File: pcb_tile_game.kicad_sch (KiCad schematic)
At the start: 40 parts, among them J1 Conn_01x05_Pin, J2 Conn_01x05_Socket, J3 Conn_01x05_Pin, J4 Conn_01x05_Socket, J5 Conn_01x05_Pin, J6 Conn_01x05_Socket, U2 ATtiny3217-M

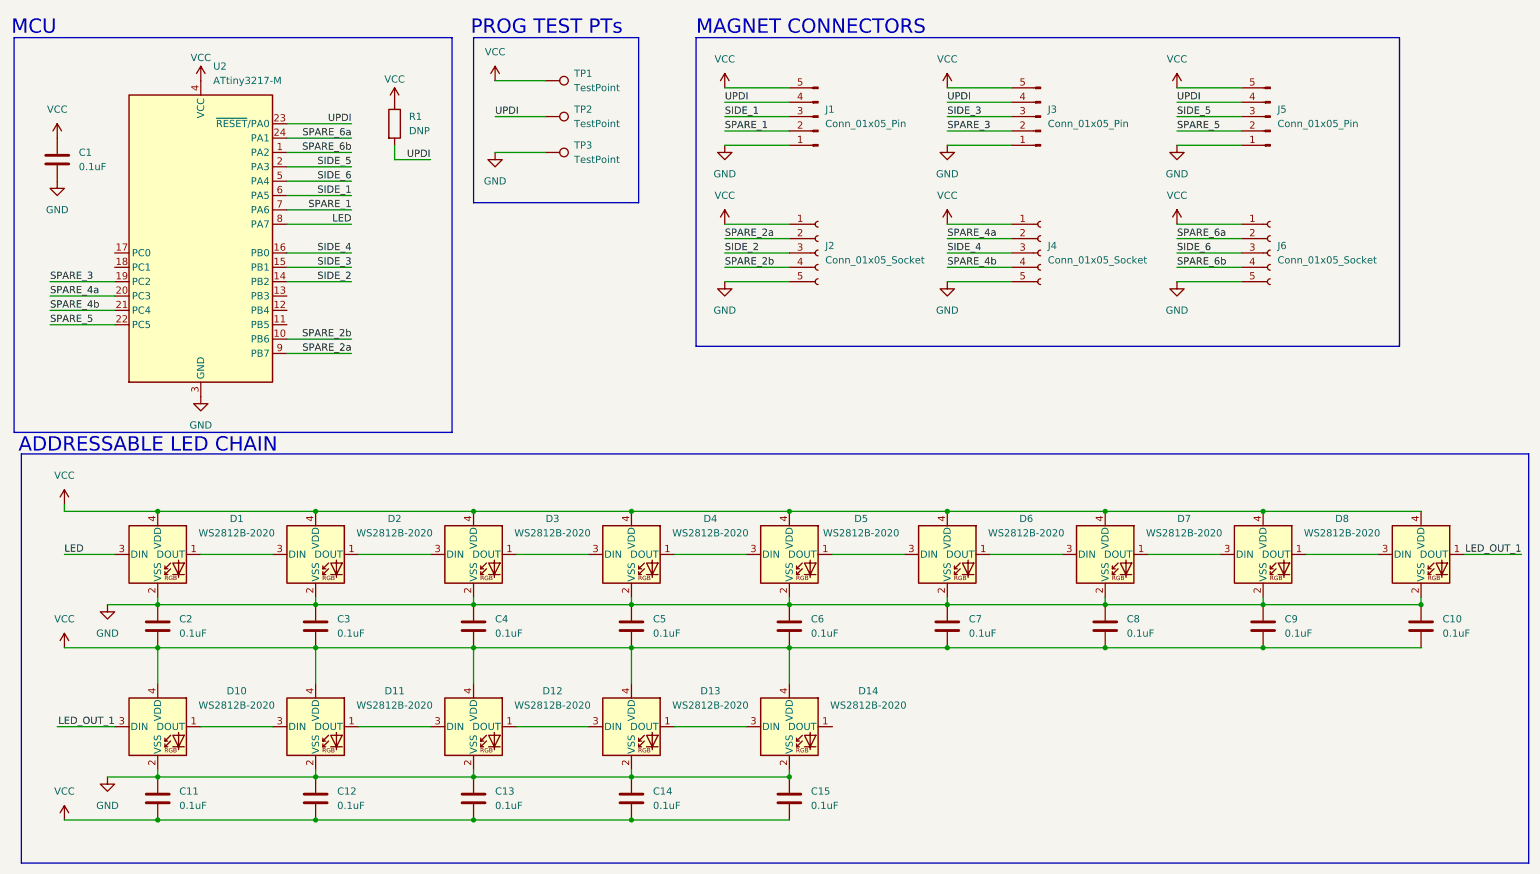
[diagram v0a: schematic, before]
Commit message: Updated pcb layout
rerouted all traces, adjusted position of LEDs and silkscreen.
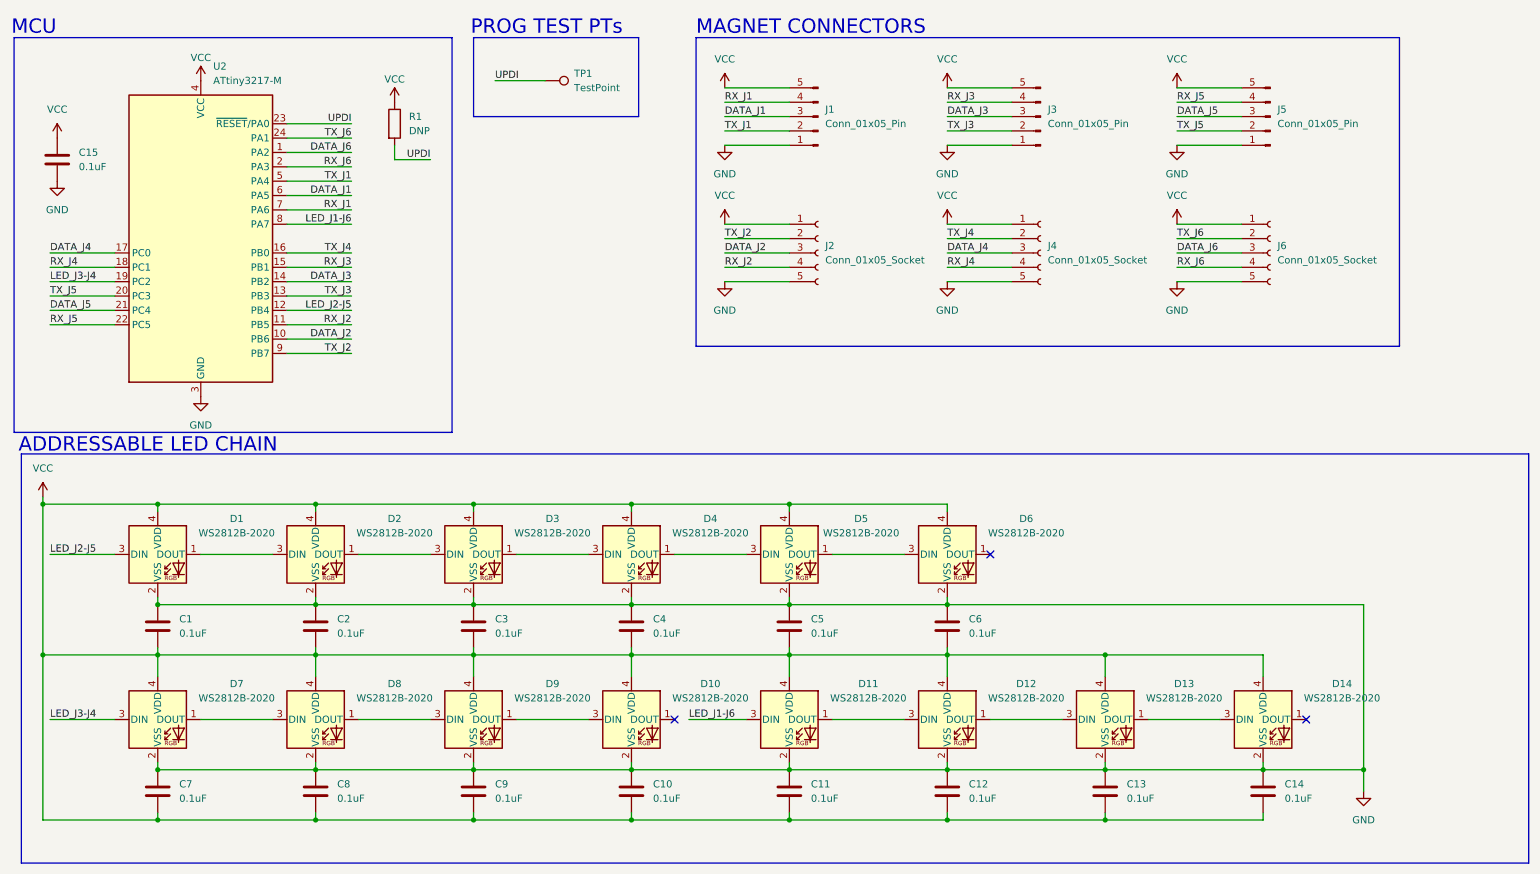
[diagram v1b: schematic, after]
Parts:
- removed TP2, TP3: TestPoint, TestPoint:TestPoint_Pad_2.0x2.0mm, symbol Connector:TestPoint
- renumbered C2 to C1, C11 to C10, C12 to C11, C13 to C12, C14 to C13, C15 to C14, C1 to C15, C3 to C2, C4 to C3, C5 to C4, C6 to C5, C7 to C6, C8 to C7, C9 to C8, C10 to C9
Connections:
- net UPDI: now also TP1.1; no longer J1.4 (Pin_4), J3.4 (Pin_4), J5.4 (Pin_4)
- net VCC: no longer TP1.1
- net at D6.1 (DOUT): no longer D7.3 (DIN)
- net at D10.1 (DOUT): no longer D11.3 (DIN)
- net RX_J2: now reaches U2.11 (PB5)
- net RX_J2: now also J2.4 (Pin_4)
- net LED_J2-J5: now reaches U2.12 (PB4)
- net LED_J2-J5: now also D1.3 (DIN)
- net TX_J3: now reaches U2.13 (PB3)
- net TX_J3: now also J3.2 (Pin_2)
- net DATA_J4: now reaches U2.17 (PC0)
- net DATA_J4: now also J4.3 (Pin_3)
- net RX_J4: now reaches U2.18 (PC1)
- net RX_J4: now also J4.4 (Pin_4)
- net LED renamed LED_J1-J6
- net LED_J1-J6: now also D11.3 (DIN); no longer D1.3 (DIN)
- net LED_OUT_1: no longer names the net of D10.3 (DIN), D9.1 (DOUT)
- net SIDE_1 renamed DATA_J1
- net SIDE_2 renamed DATA_J2
- net DATA_J2: now also U2.10 (PB6); no longer U2.14 (PB2)
- net SIDE_3 renamed DATA_J3
- net DATA_J3: now also U2.14 (PB2); no longer U2.15 (PB1)
- net SIDE_4 renamed TX_J4
- net TX_J4: now also J4.2 (Pin_2); no longer J4.3 (Pin_3)
- net SIDE_5 renamed DATA_J5
- net DATA_J5: now also U2.21 (PC4); no longer U2.2 (PA3)
- net SIDE_6 renamed DATA_J6
- net DATA_J6: now also U2.1 (PA2); no longer U2.5 (PA4)
- net SPARE_1 renamed RX_J1
- net RX_J1: now also J1.4 (Pin_4); no longer J1.2 (Pin_2)
- net SPARE_2a renamed TX_J2
- removed net SPARE_2b: J2.4 (Pin_4), U2.10 (PB6)
- net SPARE_3 renamed LED_J3-J4
- net LED_J3-J4: now also D7.3 (DIN); no longer J3.2 (Pin_2)
- net SPARE_4a renamed TX_J5
- net TX_J5: now also J5.2 (Pin_2); no longer J4.2 (Pin_2)
- removed net SPARE_4b: J4.4 (Pin_4), U2.21 (PC4)
- net SPARE_5 renamed RX_J5
- net RX_J5: now also J5.4 (Pin_4); no longer J5.2 (Pin_2)
- net SPARE_6a renamed TX_J6
- net SPARE_6b renamed RX_J6
- net RX_J6: now also U2.2 (PA3); no longer U2.1 (PA2)
- new net RX_J3: J3.4 (Pin_4), U2.15 (PB1)
- new net TX_J1: J1.2 (Pin_2), U2.5 (PA4)
- no-connect marks 0 -> 3
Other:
- moved on the sheet: C10, C11, C12, C13, C14, C7, C8, C9, D10, D11, D12, D13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
